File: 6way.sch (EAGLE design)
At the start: 7 parts

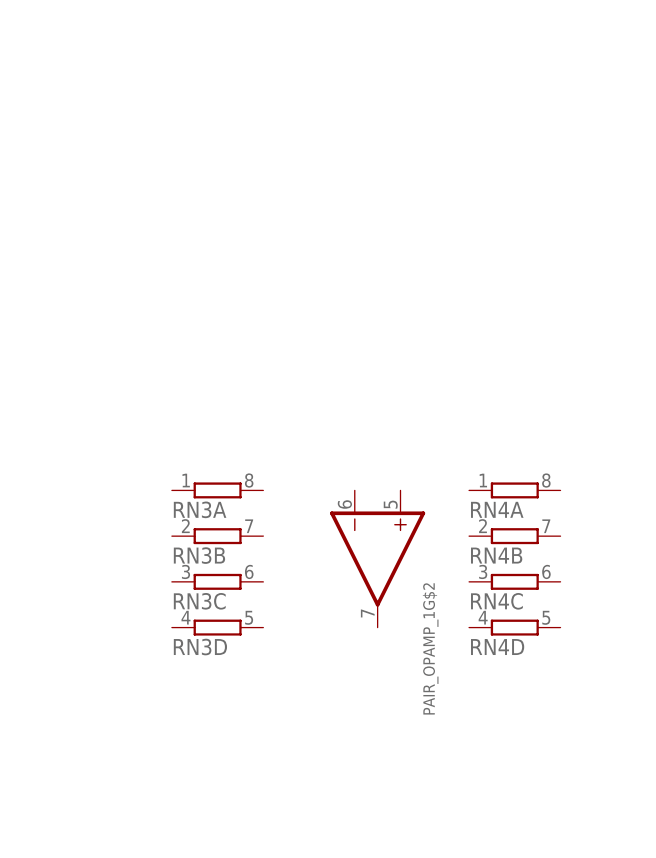
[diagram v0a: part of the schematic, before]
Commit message: sense opamps for a single pair of caps
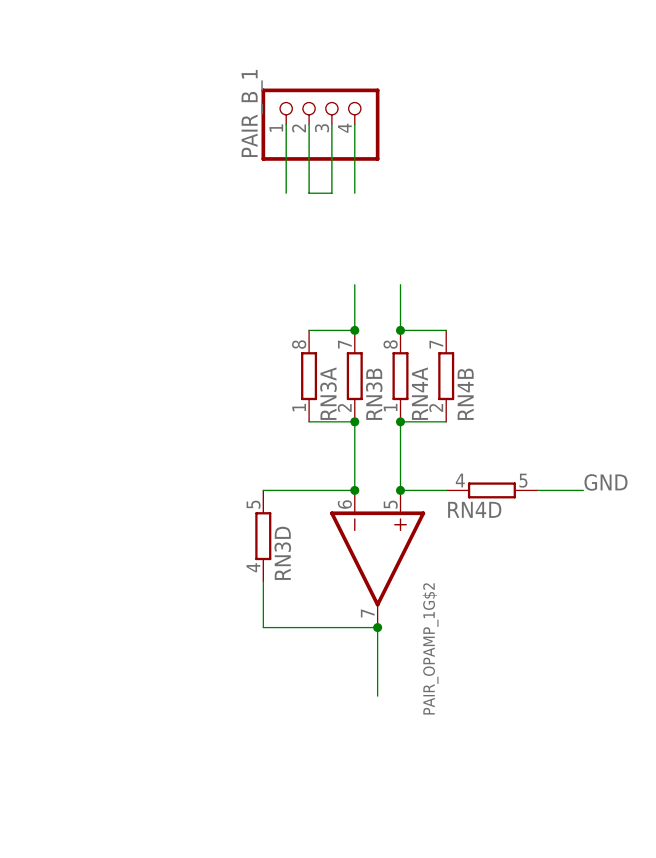
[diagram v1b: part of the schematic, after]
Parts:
- added PAIR_B_1: (no value), pinhead:PINHD-1X4
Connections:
- new net N$1: PAIR_OPAMP_1G$2.-IN, RN3A.1, RN3B.1, RN3D.2
- new net N$5: PAIR_OPAMP_1G$2.+IN, RN4A.1, RN4B.1, RN4D.1
- new net PAIR_B+_1: PAIR_B_1.1, RN4A.2, RN4B.2
- new net PAIR_B-_1: PAIR_B_1.2, PAIR_B_1.3, RN3A.2, RN3B.2
- new net PAIR_B_DISCHG_1: PAIR_B_1.4
- new net PAIR_B_SENSE_1: PAIR_OPAMP_1G$2.OUT, RN3D.1
- net GND: now also RN4D.2
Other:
- moved on the sheet: RN3A, RN3B, RN3D, RN4A, RN4B, RN4D
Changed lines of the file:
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@@
 <part name="RN3" library="resistor-dil" deviceset="4R-N" device="CAY16"/>
 <part name="RN4" library="resistor-dil" deviceset="4R-N" device="CAY16"/>
+<part name="PAIR_B_1" library="pinhead" deviceset="PINHD-1X4" device=""/>
 </parts>
 <sheets>
@@
 <instance part="RN2" gate="B" x="15.24" y="81.28" rot="R90"/>
 <instance part="RN2" gate="D" x="22.86" y="63.5" rot="R90"/>
-<instance part="RN3" gate="A" x="71.12" y="71.12"/>
-<instance part="RN3" gate="B" x="71.12" y="66.04"/>
-<instance part="RN3" gate="C" x="71.12" y="60.96"/>
-<instance part="RN3" gate="D" x="71.12" y="55.88"/>
-<instance part="RN4" gate="A" x="104.14" y="71.12"/>
-<instance part="RN4" gate="B" x="104.14" y="66.04"/>
-<instance part="RN4" gate="C" x="104.14" y="60.96"/>
-<instance part="RN4" gate="D" x="104.14" y="55.88"/>
+<instance part="RN3" gate="A" x="81.28" y="83.82" rot="R90"/>
+<instance part="RN3" gate="B" x="86.36" y="83.82" rot="R90"/>
+<instance part="RN3" gate="D" x="76.2" y="66.04" rot="R90"/>
+<instance part="RN4" gate="A" x="91.44" y="83.82" rot="R90"/>
+<instance part="RN4" gate="B" x="96.52" y="83.82" rot="R90"/>
+<instance part="RN4" gate="D" x="101.6" y="71.12"/>
+<instance part="PAIR_B_1" gate="A" x="83.82" y="114.3" rot="R90"/>
 </instances>
 <busses>
@@
 <wire x1="-12.7" y1="68.58" x2="-17.78" y2="68.58" width="0.1524" layer="91"/>
 <label x="-22.86" y="68.58" size="1.778" layer="95"/>
+</segment>
+<segment>
+<pinref part="RN4" gate="D" pin="2"/>
+<wire x1="106.68" y1="71.12" x2="111.76" y2="71.12" width="0.1524" layer="91"/>
+<label x="111.76" y="71.12" size="1.778" layer="95"/>
 </segment>
 </net>
@@
 </segment>
 </net>
+<net name="PAIR_B-_1" class="2">
+<segment>
+<pinref part="PAIR_B_1" gate="A" pin="2"/>
+<wire x1="81.28" y1="111.76" x2="81.28" y2="104.14" width="0.1524" layer="91"/>
+<pinref part="PAIR_B_1" gate="A" pin="3"/>
+<wire x1="83.82" y1="111.76" x2="83.82" y2="104.14" width="0.1524" layer="91"/>
+<wire x1="81.28" y1="104.14" x2="83.82" y2="104.14" width="0.1524" layer="91"/>
+</segment>
+<segment>
+<pinref part="RN3" gate="B" pin="2"/>
+<pinref part="RN3" gate="A" pin="2"/>
+<wire x1="86.36" y1="88.9" x2="81.28" y2="88.9" width="0.1524" layer="91"/>
+<wire x1="86.36" y1="88.9" x2="86.36" y2="93.98" width="0.1524" layer="91"/>
+<junction x="86.36" y="88.9"/>
+</segment>
+</net>
+<net name="PAIR_B_DISCHG_1" class="2">
+<segment>
+<pinref part="PAIR_B_1" gate="A" pin="4"/>
+<wire x1="86.36" y1="111.76" x2="86.36" y2="104.14" width="0.1524" layer="91"/>
+</segment>
+</net>
+<net name="PAIR_B+_1" class="2">
+<segment>
+<pinref part="PAIR_B_1" gate="A" pin="1"/>
+<wire x1="78.74" y1="111.76" x2="78.74" y2="104.14" width="0.1524" layer="91"/>
+</segment>
+<segment>
+<pinref part="RN4" gate="B" pin="2"/>
+<pinref part="RN4" gate="A" pin="2"/>
+<wire x1="96.52" y1="88.9" x2="91.44" y2="88.9" width="0.1524" layer="91"/>
+<wire x1="91.44" y1="88.9" x2="91.44" y2="93.98" width="0.1524" layer="91"/>
+<junction x="91.44" y="88.9"/>
+</segment>
+</net>
+<net name="PAIR_B_SENSE_1" class="0">
+<segment>
+<pinref part="PAIR_OPAMP_1" gate="G$2" pin="OUT"/>
+<wire x1="88.9" y1="55.88" x2="88.9" y2="48.26" width="0.1524" layer="91"/>
+<pinref part="RN3" gate="D" pin="1"/>
+<wire x1="88.9" y1="55.88" x2="76.2" y2="55.88" width="0.1524" layer="91"/>
+<wire x1="76.2" y1="55.88" x2="76.2" y2="60.96" width="0.1524" layer="91"/>
+<junction x="88.9" y="55.88"/>
+</segment>
+</net>
+<net name="N$1" class="0">
+<segment>
+<pinref part="RN3" gate="B" pin="1"/>
+<pinref part="RN3" gate="A" pin="1"/>
+<wire x1="86.36" y1="78.74" x2="81.28" y2="78.74" width="0.1524" layer="91"/>
+<pinref part="RN3" gate="D" pin="2"/>
+<pinref part="PAIR_OPAMP_1" gate="G$2" pin="-IN"/>
+<wire x1="76.2" y1="71.12" x2="86.36" y2="71.12" width="0.1524" layer="91"/>
+<wire x1="86.36" y1="71.12" x2="86.36" y2="78.74" width="0.1524" layer="91"/>
+<junction x="86.36" y="71.12"/>
+<junction x="86.36" y="78.74"/>
+</segment>
+</net>
+<net name="N$5" class="0">
+<segment>
+<pinref part="RN4" gate="B" pin="1"/>
+<pinref part="RN4" gate="A" pin="1"/>
+<wire x1="96.52" y1="78.74" x2="91.44" y2="78.74" width="0.1524" layer="91"/>
+<pinref part="PAIR_OPAMP_1" gate="G$2" pin="+IN"/>
+<wire x1="91.44" y1="71.12" x2="91.44" y2="78.74" width="0.1524" layer="91"/>
+<pinref part="RN4" gate="D" pin="1"/>
+<wire x1="96.52" y1="71.12" x2="91.44" y2="71.12" width="0.1524" layer="91"/>
+<junction x="91.44" y="71.12"/>
+<junction x="91.44" y="78.74"/>
+</segment>
+</net>

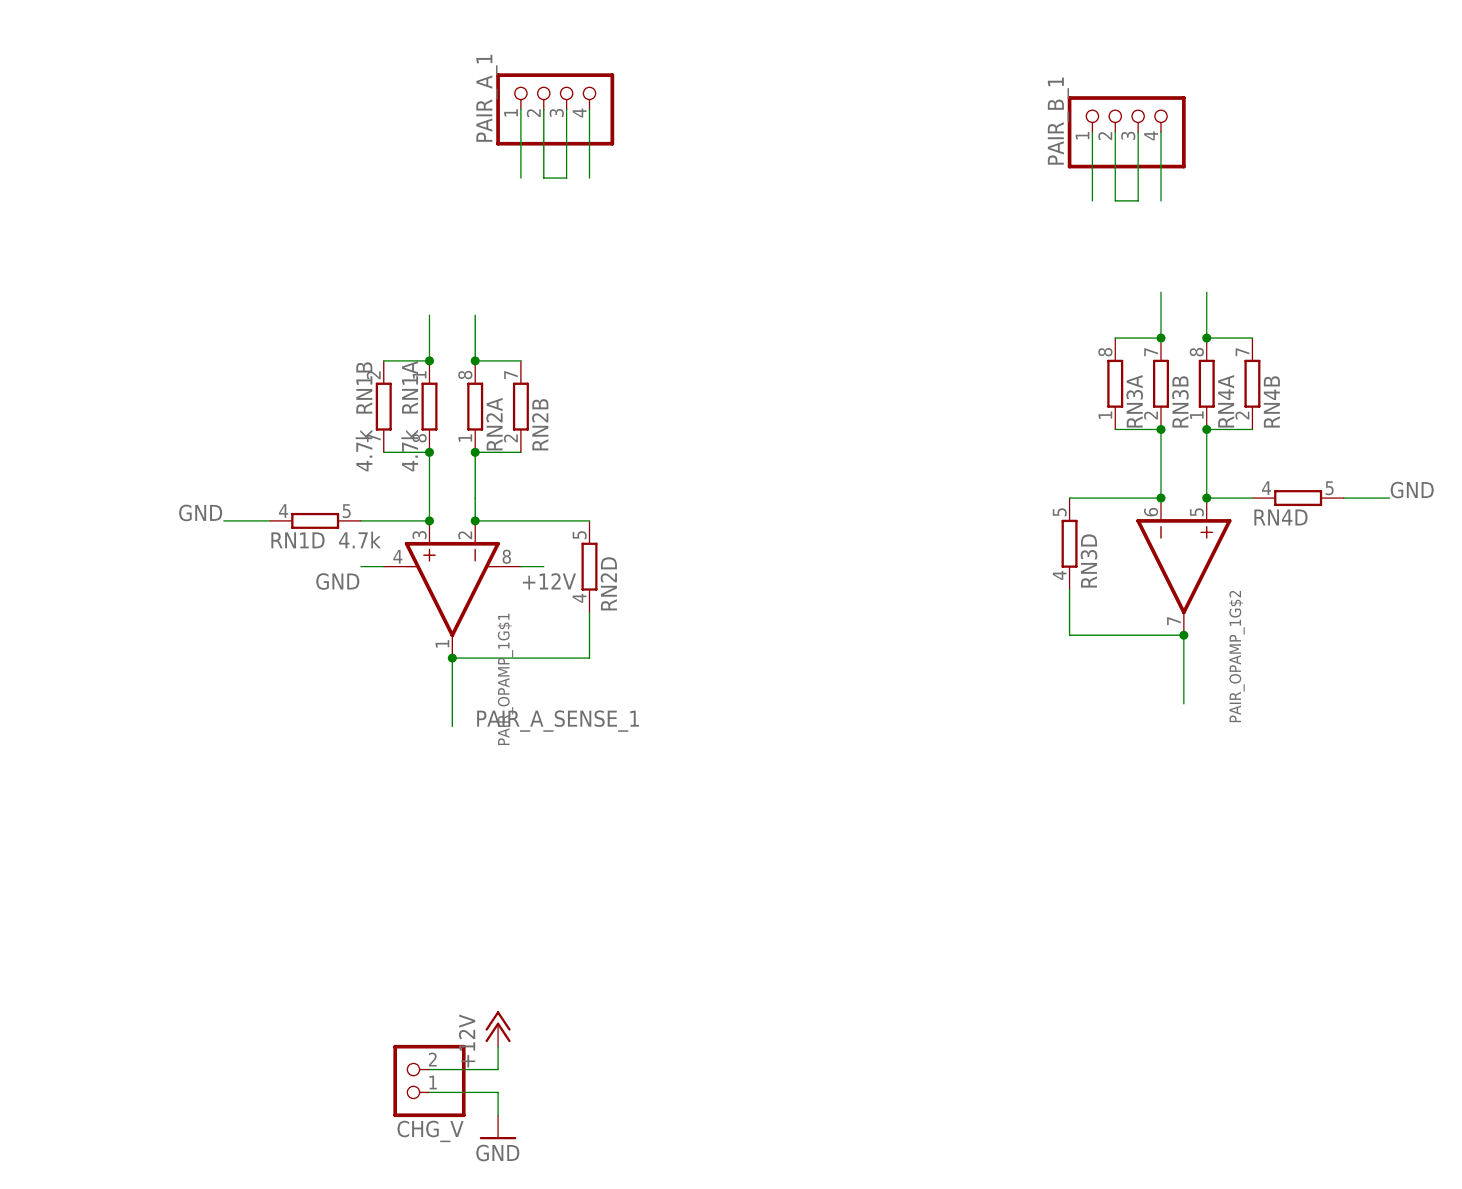
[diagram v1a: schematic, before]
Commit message: added the gatedriver from the lib
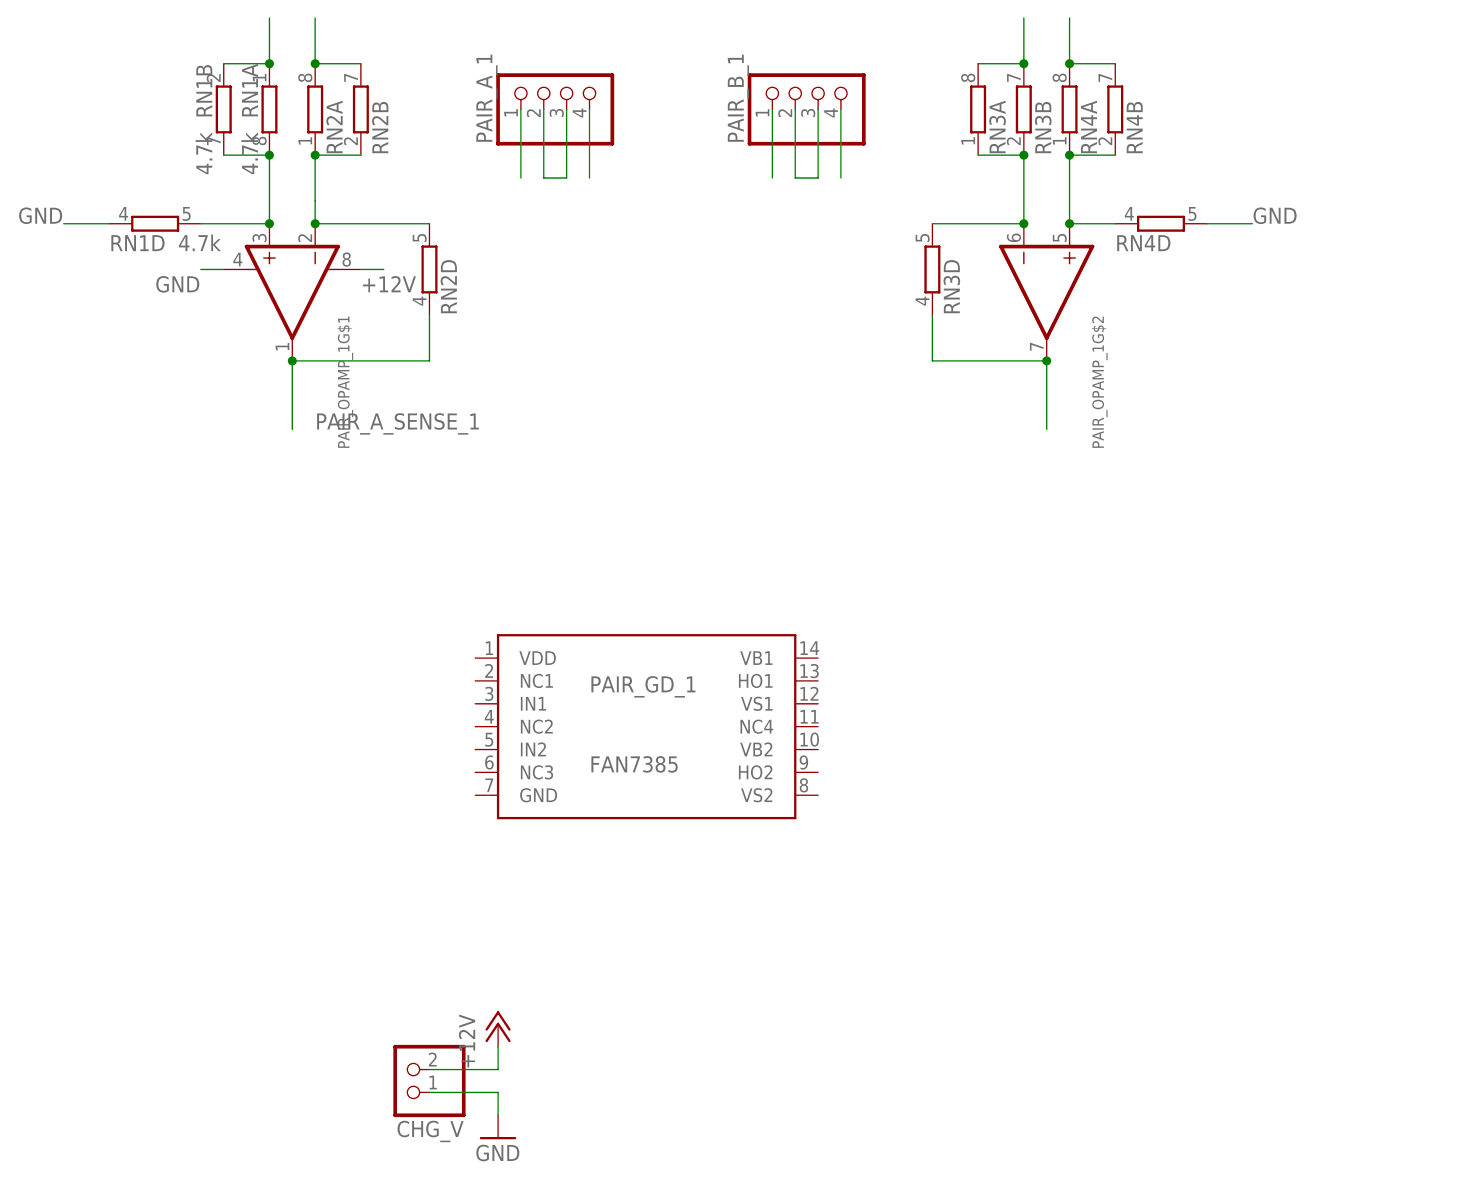
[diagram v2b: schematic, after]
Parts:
- added PAIR_GD_1: FAN7385, fan7385:FAN7385
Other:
- moved on the sheet: PAIR_B_1, PAIR_OPAMP_1G$1, PAIR_OPAMP_1G$2, RN1A, RN1B, RN1D, RN2A, RN2B, RN2D, RN3A, RN3B, RN3D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

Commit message: and added the dual-mosfet to the schematic¨
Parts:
- added PAIR_DISCHG_1: DMG9926, DMG9926:DMG9926
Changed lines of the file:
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@@
 <part name="PAIR_B_1" library="pinhead" deviceset="PINHD-1X4" device=""/>
 <part name="PAIR_GD_1" library="fan7385" deviceset="FAN7385" device=""/>
+<part name="PAIR_DISCHG_1" library="DMG9926" deviceset="DMG9926" device=""/>
 </parts>
 <sheets>
@@
 <instance part="PAIR_B_1" gate="A" x="48.26" y="116.84" rot="R90"/>
 <instance part="PAIR_GD_1" gate="G$1" x="25.4" y="45.72"/>
+<instance part="PAIR_DISCHG_1" gate="G$1" x="73.66" y="50.8"/>
 </instances>
 <busses>
 </busses>
 <nets>
-<net name="+12V" class="0">
+<net name="+12V" class="2">
 <segment>
 <pinref part="CHG_V" gate="G$1" pin="2"/>
@@
 </segment>
 </net>
-<net name="GND" class="0">
+<net name="GND" class="2">
 <segment>
 <pinref part="GND1" gate="1" pin="GND"/>
@@
 <wire x1="5.08" y1="86.36" x2="-10.16" y2="86.36" width="0.1524" layer="91"/>
 <junction x="-10.16" y="86.36"/>
-<label x="-7.62" y="78.74" size="1.778" layer="95"/>
+<label x="-33.02" y="78.74" size="1.778" layer="95"/>
 </segment>
 </net>
@@
 <wire x1="60.96" y1="86.36" x2="60.96" y2="91.44" width="0.1524" layer="91"/>
 <junction x="73.66" y="86.36"/>
+<label x="50.8" y="78.74" size="1.778" layer="95"/>
 </segment>
 </net>
